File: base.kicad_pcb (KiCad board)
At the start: 2 copper layers, 100 x 100 mm, 117 parts, among them J1 Screw_Terminal_01x02, J2 Out, Q2 MJD31C, Q3 IPD50R3K0CE, Q4 MJD31C, Q5 MMBTA42, Q6 MMBTA42, Q7 MMBTA42, Q8 MMBTA42, T1 FL2015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

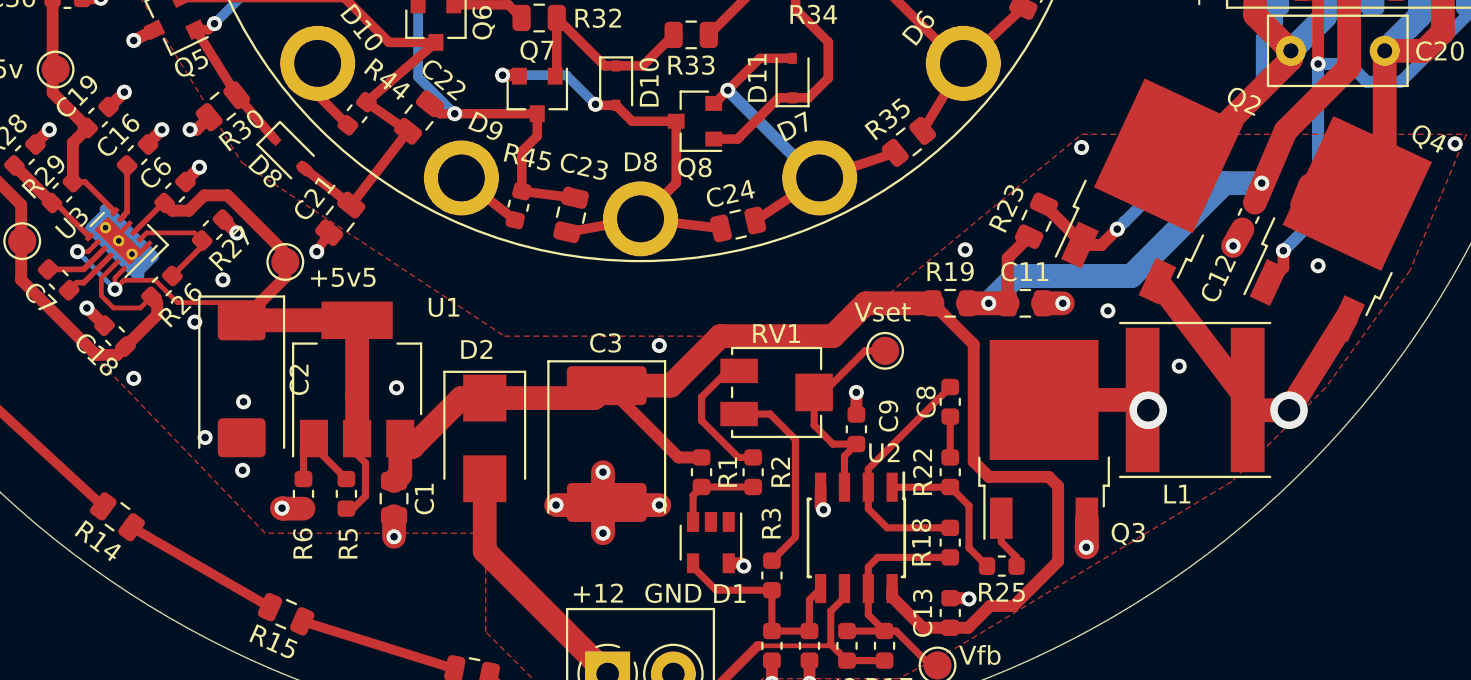
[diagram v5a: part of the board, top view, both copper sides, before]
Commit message: Added alternative L
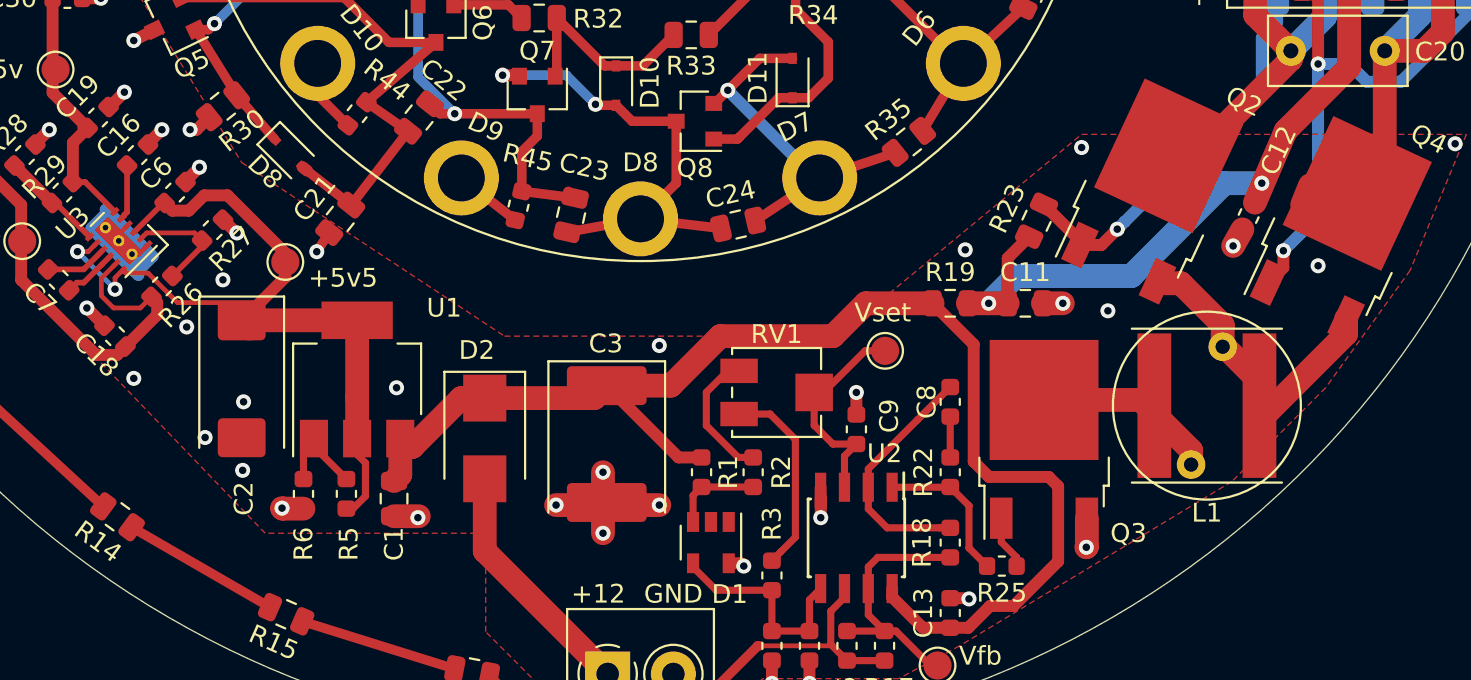
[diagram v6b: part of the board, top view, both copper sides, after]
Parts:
- added L**: L, L:L, F.Cu at (130.2, 132.0)
- moved L1 0.69 mm to (130.2, 132.0)
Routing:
- net Net-(L1-Pad2): track 5.78 -> 9.70 mm, vias 1 -> 0
- net GND: track 154.7 -> 155.7 mm, vias 49 -> 48
- net Net-(L1-Pad1): track 16.1 -> 15.7 mm, vias 1 -> 0
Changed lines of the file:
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@@
     (tracks 558)
     (zones 0)
-    (modules 117)
+    (modules 118)
     (nets 69)
   )
@@
   )
   (setup
-    (last_trace_width 1.27)
+    (last_trace_width 0.254)
     (user_trace_width 0.254)
     (user_trace_width 0.3048)
@@
     (add_net "Net-(U4-Pad8)")
   )
+  (module L:L (layer F.Cu)
+    (at 130.175 131.953 75)
+    (fp_text reference L** (at 0.25 5.75 75) (layer F.SilkS) hide
+      (effects (font (size 1 1) (thickness 0.15)))
+    )
+    (fp_text value L (at 0 -5.75 75) (layer F.Fab)
+      (effects (font (size 1 1) (thickness 0.15)))
+    )
+    (fp_circle (center 0 0) (end 0.25 5) (layer F.SilkS) (width 0.12))
+    (pad 2 thru_hole circle (at -3.25 0 75) (size 1.524 1.524) (drill 0.762) (layers *.Cu *.Mask)
+      (net 33 "Net-(L1-Pad2)"))
+    (pad 1 thru_hole circle (at 3.25 0 75) (size 1.524 1.524) (drill 0.762) (layers *.Cu *.Mask)
+      (net 32 "Net-(L1-Pad1)"))
+  )
   (module slots:ISlot (layer F.Cu)
     (at 82.2 78.8 225)
@@
     (tags "capacitor tantalum")
     (attr smd)
-    (fp_text reference C2 (at 0 -3.1 270) (layer F.SilkS)
+    (fp_text reference C2 (at 6.356 -0.117 270) (layer F.SilkS)
       (effects (font (size 1 1) (thickness 0.15)))
     )
@@
     (tags capacitor)
     (attr smd)
-    (fp_text reference C1 (at 0 -1.65 270) (layer F.SilkS)
+    (fp_text reference C1 (at 2.413 0 270) (layer F.SilkS)
       (effects (font (size 1 1) (thickness 0.15)))
     )
@@
     (tags capacitor)
     (attr smd)
-    (fp_text reference C12 (at 3.71232 0.034321 245) (layer F.SilkS)
+    (fp_text reference C12 (at -3.829239 0.036749 245) (layer F.SilkS)
       (effects (font (size 1 1) (thickness 0.15)))
     )
@@
   )
   (module Inductor_SMD:L_Taiyo-Yuden_NR-80xx (layer F.Cu)
-    (at 129.55 131.65 180)
+    (at 130.175 131.953 180)
     (descr "Inductor, Taiyo Yuden, NR series, Taiyo-Yuden_NR-80xx, 8.0mmx8.0mm")
     (tags "inductor taiyo-yuden nr smd")
     (attr smd)
-    (fp_text reference L1 (at 0.95 -5.05 180) (layer F.SilkS)
+    (fp_text reference L1 (at 0 -5.715 180) (layer F.SilkS)
       (effects (font (size 1 1) (thickness 0.15)))
     )
@@
   (via (at 123.75 139.5) (size 0.8) (drill 0.4) (layers F.Cu B.Cu) (net 2))
   (via (at 117.5 142.25) (size 0.8) (drill 0.4) (layers F.Cu B.Cu) (net 2))
-  (via (at 109.75 137.5) (size 0.8) (drill 0.4) (layers F.Cu B.Cu) (net 2))
+  (via (at 109.601 137.922) (size 0.8) (drill 0.4) (layers F.Cu B.Cu) (net 2))
   (via (at 105.5 140.5) (size 0.8) (drill 0.4) (layers F.Cu B.Cu) (net 2))
   (via (at 98 135.5) (size 0.8) (drill 0.4) (layers F.Cu B.Cu) (net 2))
@@
   (segment (start 105.35 140.35) (end 105.5 140.5) (width 0.635) (layer F.Cu) (net 2))
   (segment (start 104.7 140.35) (end 105.35 140.35) (width 0.635) (layer F.Cu) (net 2))
-  (segment (start 109.595 137.345) (end 109.75 137.5) (width 0.635) (layer F.Cu) (net 2))
   (segment (start 109.595 136.3) (end 109.595 137.345) (width 0.635) (layer F.Cu) (net 2))
   (via (at 111.5 131.25) (size 0.8) (drill 0.4) (layers F.Cu B.Cu) (net 2))
@@
   (via (at 101 128.75) (size 0.8) (drill 0.4) (layers F.Cu B.Cu) (net 2))
   (via (at 73 130.5) (size 0.8) (drill 0.4) (layers F.Cu B.Cu) (net 2))
-  (via (at 76.25 127.5) (size 0.8) (drill 0.4) (layers F.Cu B.Cu) (net 2))
+  (via (at 75.819 127.762) (size 0.8) (drill 0.4) (layers F.Cu B.Cu) (net 2))
   (via (at 77.75 125.25) (size 0.8) (drill 0.4) (layers F.Cu B.Cu) (net 2))
   (via (at 87 131) (size 0.8) (drill 0.4) (layers F.Cu B.Cu) (net 2))
@@
   (via (at 143.4 118) (size 0.8) (drill 0.4) (layers F.Cu B.Cu) (net 2))
   (via (at 123.5 118.2) (size 0.8) (drill 0.4) (layers F.Cu B.Cu) (net 2))
-  (via (at 128.7 129.85) (size 0.8) (drill 0.4) (layers F.Cu B.Cu) (net 2))
   (via (at 124.9 126.9) (size 0.8) (drill 0.4) (layers F.Cu B.Cu) (net 2))
   (via (at 131.572 123.444) (size 0.8) (drill 0.4) (layers F.Cu B.Cu) (net 2))
   (via (at 117.3 123.65) (size 0.8) (drill 0.4) (layers F.Cu B.Cu) (net 2))
   (segment (start 131.572 123.444) (end 132.067188 122.563717) (width 1.27) (layer F.Cu) (net 2))
-  (via (at 86.868 138.938) (size 0.8) (drill 0.4) (layers F.Cu B.Cu) (net 2))
+  (via (at 88.138 137.922) (size 0.8) (drill 0.4) (layers F.Cu B.Cu) (net 2))
   (via (at 80.899 137.414) (size 0.8) (drill 0.4) (layers F.Cu B.Cu) (net 2))
-  (segment (start 86.868 137.8435) (end 86.868 138.938) (width 1.27) (layer F.Cu) (net 2))
   (segment (start 80.9245 137.4395) (end 80.899 137.414) (width 1.27) (layer F.Cu) (net 2))
   (segment (start 82.042 137.4395) (end 80.9245 137.4395) (width 1.27) (layer F.Cu) (net 2))
+  (segment (start 86.868 137.8435) (end 88.187045 137.8435) (width 1.27) (layer F.Cu) (net 2))
+  (segment (start 109.601 137.922) (end 109.601 136.852848) (width 0.635) (layer F.Cu) (net 2))
   (segment (start 74.643153 121.143153) (end 74.643153 121.156847) (width 0.635) (layer F.Cu) (net 3))
   (segment (start 74.571706 121.156847) (end 74.643153 121.156847) (width 0.3048) (layer F.Cu) (net 3))
@@
   (segment (start 72 125.142767) (end 72.412132 124.730635) (width 0.254) (layer F.Cu) (net 3))
   (segment (start 72 125.75) (end 72 125.142767) (width 0.254) (layer F.Cu) (net 3))
-  (segment (start 74.142699 125.275211) (end 72.474789 125.275211) (width 0.254) (layer F.Cu) (net 3))
-  (segment (start 75.329988 126.4625) (end 74.142699 125.275211) (width 0.254) (layer F.Cu) (net 3))
-  (segment (start 72.399999 125.350001) (end 72 125.75) (width 0.254) (layer F.Cu) (net 3))
-  (segment (start 72.474789 125.275211) (end 72.399999 125.350001) (width 0.254) (layer F.Cu) (net 3))
-  (segment (start 79.7 126.4625) (end 75.329988 126.4625) (width 0.254) (layer F.Cu) (net 3))
   (segment (start 81.075 124.3) (end 81.075 124.509) (width 0.381) (layer F.Cu) (net 3))
   (segment (start 81.075 125.0875) (end 79.7 126.4625) (width 0.381) (layer F.Cu) (net 3))
@@
   (segment (start 84.328 137.4395) (end 84.6835 137.4395) (width 0.381) (layer F.Cu) (net 3))
   (segment (start 84.6835 137.4395) (end 85.344 136.779) (width 0.381) (layer F.Cu) (net 3))
+  (segment (start 75.329988 126.4625) (end 79.7 126.4625) (width 0.254) (layer F.Cu) (net 3))
+  (segment (start 73.757221 124.889733) (end 75.329988 126.4625) (width 0.254) (layer F.Cu) (net 3))
+  (segment (start 72.57123 124.889733) (end 73.757221 124.889733) (width 0.254) (layer F.Cu) (net 3))
+  (segment (start 72.412132 124.730635) (end 72.57123 124.889733) (width 0.254) (layer F.Cu) (net 3))
   (segment (start 109 142.295) (end 109 143.9625) (width 0.381) (layer F.Cu) (net 4))
   (segment (start 109.595 141.7) (end 109 142.295) (width 0.381) (layer F.Cu) (net 4))
@@
   (segment (start 68.75 94.0625) (end 68.75 93.25) (width 0.508) (layer F.Cu) (net 31))
   (segment (start 67.5 92) (end 67.5 88.75) (width 0.508) (layer F.Cu) (net 31))
-  (via (at 134.55 132.2) (size 2) (drill 1.2) (layers F.Cu B.Cu) (net 32))
-  (segment (start 132.9 132.2) (end 132.35 131.65) (width 1.27) (layer F.Cu) (net 32))
-  (segment (start 134.55 132.2) (end 132.9 132.2) (width 1.27) (layer F.Cu) (net 32))
-  (segment (start 137.591385 127.320062) (end 134.55 132.2) (width 1.27) (layer F.Cu) (net 32))
-  (segment (start 127.541385 125.320062) (end 132.35 131.65) (width 1.27) (layer F.Cu) (net 32))
-  (via (at 127.05 132.2) (size 2) (drill 1.2) (layers F.Cu B.Cu) (net 33))
-  (segment (start 126.5 131.65) (end 127.05 132.2) (width 1.27) (layer F.Cu) (net 33))
-  (segment (start 121.5 131.65) (end 126.5 131.65) (width 1.27) (layer F.Cu) (net 33))
+  (segment (start 137.591385 128.129811) (end 133.413849 132.307347) (width 1.27) (layer F.Cu) (net 32))
+  (segment (start 137.591385 127.320062) (end 137.591385 128.129811) (width 1.27) (layer F.Cu) (net 32))
+  (segment (start 132.975 130.666388) (end 131.148768 128.840156) (width 1.27) (layer F.Cu) (net 32))
+  (segment (start 132.975 131.953) (end 132.975 130.666388) (width 1.27) (layer F.Cu) (net 32))
+  (segment (start 131.016162 128.813741) (end 131.016162 127.661239) (width 1.27) (layer F.Cu) (net 32))
+  (segment (start 128.786445 125.431522) (end 127.93332 125.431522) (width 1.27) (layer F.Cu) (net 32))
+  (segment (start 131.016162 127.661239) (end 128.786445 125.431522) (width 1.27) (layer F.Cu) (net 32))
+  (segment (start 126.648186 131.65) (end 121.5 131.65) (width 1.27) (layer F.Cu) (net 33))
+  (segment (start 129.333838 135.092259) (end 129.333838 134.335652) (width 1.27) (layer F.Cu) (net 33))
+  (segment (start 129.333838 134.335652) (end 126.648186 131.65) (width 1.27) (layer F.Cu) (net 33))
   (segment (start 104.186161 77.390703) (end 100 78) (width 0.508) (layer F.Cu) (net 34))
   (segment (start 100 83.388) (end 98.600847 84.787153) (width 0.508) (layer F.Cu) (net 34))
@@
   (segment (start 136.1 113.75) (end 137.75 113.75) (width 0.635) (layer B.Cu) (net 47))
   (segment (start 137.75 113.75) (end 138.7 114.7) (width 0.635) (layer B.Cu) (net 47))
-  (segment (start 103.25 132.752902) (end 105.209598 134.7125) (width 0.381) (layer F.Cu) (net 48))
   (segment (start 105.209598 134.7125) (end 106 134.7125) (width 0.381) (layer F.Cu) (net 48))
-  (segment (start 103.25 131.5) (end 103.25 132.752902) (width 0.381) (layer F.Cu) (net 48))
+  (segment (start 103.505 133.007902) (end 105.209598 134.7125) (width 0.381) (layer F.Cu) (net 48))
+  (segment (start 103.505 131.245) (end 103.505 133.007902) (width 0.381) (layer F.Cu) (net 48))
   (segment (start 105.25 130.1) (end 104.65 130.1) (width 0.381) (layer F.Cu) (net 48))
-  (segment (start 104.65 130.1) (end 103.25 131.5) (width 0.381) (layer F.Cu) (net 48))
+  (segment (start 104.65 130.1) (end 103.505 131.245) (width 0.381) (layer F.Cu) (net 48))
   (segment (start 108.25 138.9625) (end 107.461612 139.750888) (width 0.381) (layer F.Cu) (net 49))
   (segment (start 107.461612 139.750888) (end 107 140.2125) (width 0.381) (layer F.Cu) (net 49))
